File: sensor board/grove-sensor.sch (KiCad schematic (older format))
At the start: 28 parts, among them P1 CONN_01X03, P2 CONN_01X03, P3 CONN_01X03, P4 CONN_01X04, Q1 PN2222A, U1 ADD8704, U2 SI1143, U3 Teensy_3.1

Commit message: bunch of sensor stuff
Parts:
- removed P1, P2, P3: CONN_01X03, symbol CONN_01X03
- removed P4: CONN_01X04, symbol CONN_01X04
- added P1, P10, P11, P12, P13, P2, P3, P4, P5, P6, P7, P8, P9: CONN_01X01, Pin_Headers:Pin_Header_Straight_1x01, symbol CONN_01X01
- C1, C2, C3: footprint (none) -> Capacitors_SMD:C_0603_HandSoldering
- D1, D2, D3: footprint (none) -> LEDs:LED_0805
- Q1: footprint (none) -> TO_SOT_Packages_SMD:SOT-23_Handsoldering
- R1, R10, R11, R12, R13, R14, R3, R4, R6, R7, R8, R9: footprint (none) -> Resistors_SMD:R_0603_HandSoldering
- R2, R5: footprint (none) -> Resistors_SMD:R_0402
- U1: footprint (none) -> SI1143:TSSOP-14
- U2: footprint (none) -> SI1143:SI1143
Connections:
- wire segments 97 -> 98

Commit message: Some fixes and placement changes
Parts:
- removed P2, P3, P4, P5, P6: CONN_01X01, Pin_Headers:Pin_Header_Straight_1x01, symbol CONN_01X01
- added D4, D5: LED_RGB, LEDs:LED_WS2812-PLCC6, symbol LED_RGB
- added R15, R16, R17, R18, R19, R20: 100, Resistors_SMD:R_0603_HandSoldering, symbol R
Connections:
- net +5V: no longer P1.1 (P1)
- net GND: now also D4.1 (RC), D4.2 (GC), D4.3 (BC), D5.1 (RC), D5.2 (GC), D5.3 (BC)
- net OUT: no longer C2.1, R13.2
- net PIR_IN: now reaches U3.20 (20/A6)
- net PIR_IN: now also P1.1 (P1)
- net LED1_R: now reaches U3.4 (4(RX))
- net LED1_R: now also R18.1
- net LED1_G: now reaches U3.5
- net LED1_G: now also R19.1
- net LED1_B: now reaches U3.6
- net LED1_B: now also R20.1
- net LED2_R: now reaches U3.7 (7(RX3))
- net LED2_R: now also R15.1
- net LED2_G: now reaches U3.8 (8(TX3))
- net LED2_G: now also R16.1
- net LED2_B: now reaches U3.9 (9(RX2))
- net LED2_B: now also R17.1
- net at R5.1, R6.2, U1.3 (+INA): now also R7.2
- net at R12.1, U1.8 (OUTC): now also C2.1, R13.2
- net PROX_INT: no longer names the net of U2.4 (INT)
- new net: D5.4 (BA), R20.2
- new net: D5.5 (GA), R19.2
- new net: D5.6 (RA), R18.2
- new net: D4.4 (BA), R17.2
- new net: D4.5 (GA), R16.2
- new net: D4.6 (RA), R15.2
- no-connect marks 2 -> 3
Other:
- moved on the sheet: P10, P11, P12, P13, R12

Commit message: Draft sensor route on 4 layers
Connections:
- net LED1_B: now also U3.4 (4(RX)); no longer U3.6
- net LED1_R: now also U3.6; no longer U3.4 (4(RX))
- net LED2_B: now also U3.7 (7(RX3)); no longer U3.9 (9(RX2))
- net LED2_R: now also U3.9 (9(RX2)); no longer U3.7 (7(RX3))
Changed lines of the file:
@@
 Wire Wire Line
 	9150 1150 9350 1150
-Text Label 7600 2500 0    60   ~ 0
+Text Label 7600 2800 0    60   ~ 0
 LED1_R
 Text Label 7600 2650 0    60   ~ 0
 LED1_G
-Text Label 7600 2800 0    60   ~ 0
+Text Label 7600 2500 0    60   ~ 0
 LED1_B
-Text Label 7600 2950 0    60   ~ 0
+Text Label 7600 3250 0    60   ~ 0
 LED2_R
 Text Label 7600 3100 0    60   ~ 0
 LED2_G
-Text Label 7600 3250 0    60   ~ 0
+Text Label 7600 2950 0    60   ~ 0
 LED2_B
 Wire Wire Line

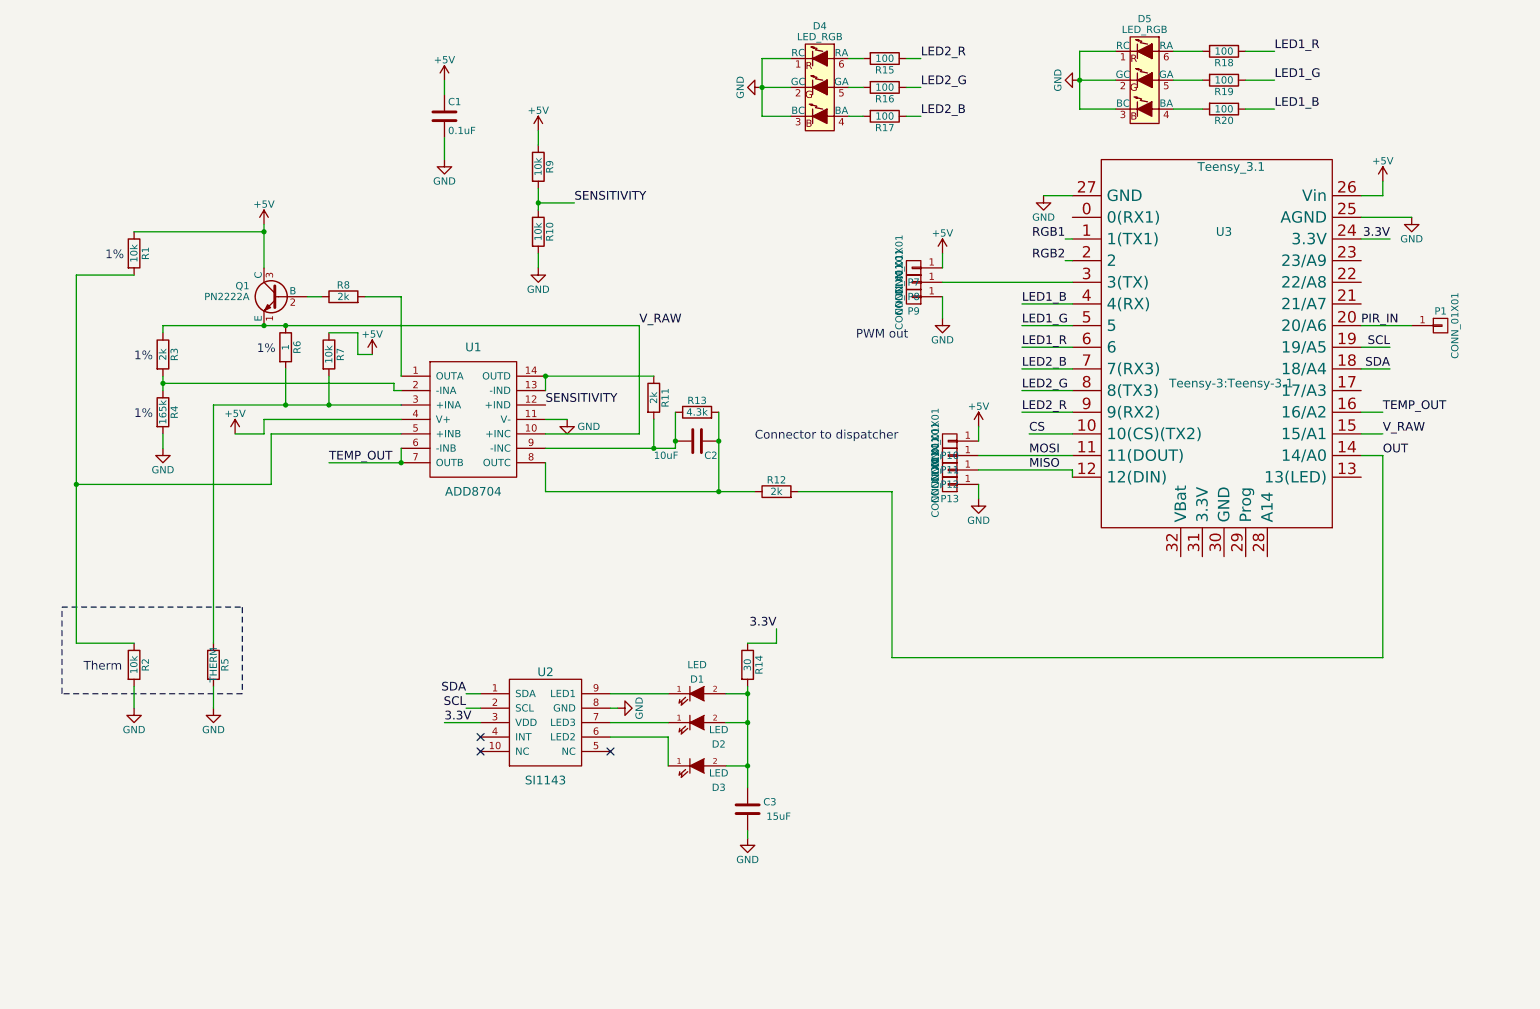
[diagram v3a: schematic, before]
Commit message: Fixes and updates to sensor board
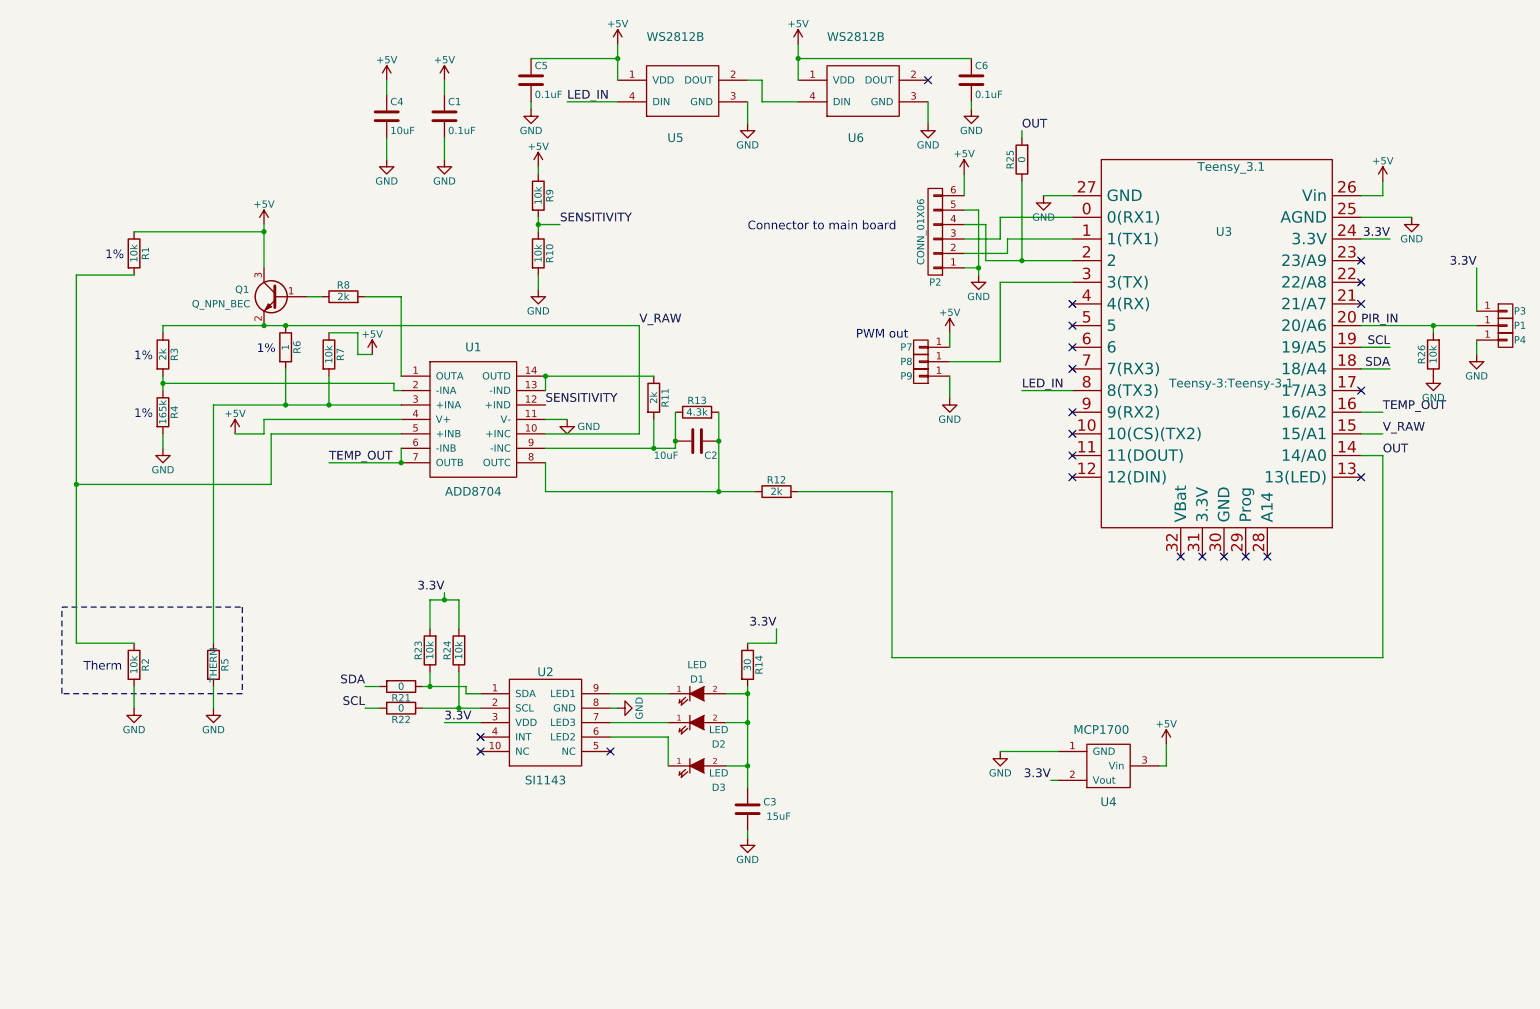
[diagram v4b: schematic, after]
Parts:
- removed D4, D5: LED_RGB, LEDs:LED_WS2812-PLCC6, symbol LED_RGB
- removed P10, P11, P12, P13: CONN_01X01, Pin_Headers:Pin_Header_Straight_1x01, symbol CONN_01X01
- removed Q1: PN2222A, TO_SOT_Packages_SMD:SOT-23_Handsoldering, symbol PN2222A
- removed R15, R16, R17, R18, R19, R20: 100, Resistors_SMD:R_0603_HandSoldering, symbol R
- added C4: 10uF, Capacitors_SMD:C_0603_HandSoldering, symbol C
- added C5, C6: 0.1uF, Capacitors_SMD:C_0603_HandSoldering, symbol C
- added P2: CONN_01X06, Pin_Headers:Pin_Header_Straight_1x06, symbol CONN_01X06
- added P3, P4: CONN_01X01, Pin_Headers:Pin_Header_Straight_1x01, symbol CONN_01X01
- added Q1: Q_NPN_BEC, TO_SOT_Packages_SMD:SOT-23, symbol Q_NPN_BEC
- added R21, R22, R25: 0, Resistors_SMD:R_0603_HandSoldering, symbol R
- added R23, R24, R26: 10k, Resistors_SMD:R_0603_HandSoldering, symbol R
- added U4: MCP1700, TO_SOT_Packages_SMD:SOT-23, symbol MCP1700
- added U5, U6: WS2812B, LEDs:LED_WS2812B-PLCC4, symbol WS2812B
- R2: footprint Resistors_SMD:R_0402 -> Resistors_SMD:R_0603
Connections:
- net +5V: now also C4.1, C5.1, C6.1, P2.6 (P6), Q1.3 (C), U4.3 (Vin), U5.1 (VDD), U6.1 (VDD)
- net 3.3V: now also P3.1 (P1), R23.2, R24.2, U4.2 (Vout)
- net GND: now also C4.2, C5.2, C6.2, P2.1 (P1), P2.5 (P5), P4.1 (P1), R26.1, U4.1 (GND), U5.3 (GND), U6.3 (GND)
- net OUT: now also R25.2
- net PIR_IN: now also R26.2
- net SCL: now also R22.2; no longer U2.2 (SCL)
- net SDA: now also R21.2; no longer U2.1 (SDA)
- net V_RAW: now also Q1.2 (E)
- net at U3.0 (0(RX1)): now also P2.3 (P3)
- net at R8.1: now also Q1.1 (B)
- net CS: no longer names the net of U3.10 (10(CS)(TX2))
- net LED1_B: no longer names the net of U3.4 (4(RX))
- net LED1_G: no longer names the net of U3.5
- net LED1_R: no longer names the net of U3.6
- net LED2_B: no longer names the net of U3.7 (7(RX3))
- net LED2_G renamed LED_IN
- net LED_IN: now also U5.4 (DIN)
- net LED2_R: no longer names the net of U3.9 (9(RX2))
- net MISO: no longer names the net of U3.12 (12(DIN))
- net MOSI: no longer names the net of U3.11 (11(DOUT))
- net RGB1: no longer names the net of U3.1 (1(TX1))
- net RGB1: now also P2.2 (P2)
- net RGB2: no longer names the net of U3.2
- net RGB2: now also P2.4 (P4), R25.1
- new net: R21.1, R23.1, U2.1 (SDA)
- new net: R22.1, R24.1, U2.2 (SCL)
- new net: U5.2 (DOUT), U6.4 (DIN)
- no-connect marks 3 -> 22
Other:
- note added: "Connector to main board\n"
- note removed: "Connector to dispatcher"
- moved on the sheet: P1, P7, P8, P9, R10, R9

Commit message: Changes for rev 2 of sensor board
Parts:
- removed P1, P3, P4, P7, P8, P9: CONN_01X01, Pin_Headers:Pin_Header_Straight_1x01, symbol CONN_01X01
- added P1, P3: CONN_01X03, Pin_Headers:Pin_Header_Straight_1x03, symbol CONN_01X03
- added P5, P6: CONN_01X01, Pin_Headers:Pin_Header_Straight_1x01, symbol CONN_01X01
- added R15: 300, Resistors_SMD:R_0603_HandSoldering, symbol R
- C4: value 10uF -> 100uF; footprint Capacitors_SMD:C_0603_HandSoldering -> Capacitors_SMD:C_1210_HandSoldering
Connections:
- net +5V: now also P1.3 (P3), P3.1 (P1)
- net GND: now also P1.1 (P1), P3.3 (P3)
- net LED_IN: now also R15.1; no longer U3.8 (8(TX3))
- net PIR_IN: now also P3.2 (P2)
- net at U3.3 (3(TX)): now also P1.2 (P2)
- new net: R15.2, U3.8 (8(TX3))
- no-connect marks 22 -> 24
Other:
- note added: "Mounting holes (M3)\n"
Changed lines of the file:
@@
 	1    0    0    -1
 $EndComp
-Text Notes 6450 2750 0    60   ~ 0
+Text Notes 6350 2950 0    60   ~ 0
 PWM out\n
 $Comp
@@
 	1    0    0    -1
 $EndComp
-$Comp
-L CONN_01X01 P7
-U 1 1 576CE696
-P 6900 2800
-F 0 "P7" H 7000 2800 50  0000 C CNN
-F 1 "CONN_01X01" H 7300 2800 50  0001 C CNN
-F 2 "Pin_Headers:Pin_Header_Straight_1x01" H 6900 2800 50  0001 C CNN
-F 3 "" H 6900 2800 50  0000 C CNN
-	1    6900 2800
-	-1   0    0    1
-$EndComp
-$Comp
-L CONN_01X01 P8
-U 1 1 576CE71E
-P 6900 2900
-F 0 "P8" H 7000 2900 50  0000 C CNN
-F 1 "CONN_01X01" H 7300 2900 50  0001 C CNN
-F 2 "Pin_Headers:Pin_Header_Straight_1x01" H 6900 2900 50  0001 C CNN
-F 3 "" H 6900 2900 50  0000 C CNN
-	1    6900 2900
-	-1   0    0    1
-$EndComp
-$Comp
-L CONN_01X01 P9
-U 1 1 576CE79F
-P 6900 3000
-F 0 "P9" H 7000 3000 50  0000 C CNN
-F 1 "CONN_01X01" H 7300 3000 50  0001 C CNN
-F 2 "Pin_Headers:Pin_Header_Straight_1x01" H 6900 3000 50  0001 C CNN
-F 3 "" H 6900 3000 50  0000 C CNN
-	1    6900 3000
-	-1   0    0    1
-$EndComp
 NoConn ~ 3850 5500
 Text Label 9950 2650 0    60   ~ 0
 PIR_IN
-$Comp
-L CONN_01X01 P1
-U 1 1 577554A8
-P 10950 2650
-F 0 "P1" H 11050 2650 50  0000 C CNN
-F 1 "CONN_01X01" V 11050 2650 50  0001 C CNN
-F 2 "Pin_Headers:Pin_Header_Straight_1x01" H 10950 2650 50  0001 C CNN
-F 3 "" H 10950 2650 50  0000 C CNN
-	1    10950 2650
-	1    0    0    -1
-$EndComp
 NoConn ~ 9950 3700
 NoConn ~ 9950 3100
@@
 P 3200 1200
 F 0 "C4" H 3225 1300 50  0000 L CNN
-F 1 "10uF" H 3225 1100 50  0000 L CNN
-F 2 "Capacitors_SMD:C_0603_HandSoldering" H 3238 1050 50  0001 C CNN
+F 1 "100uF" H 3225 1100 50  0000 L CNN
+F 2 "Capacitors_SMD:C_1210_HandSoldering" H 3238 1050 50  0001 C CNN
 F 3 "" H 3200 1200 50  0000 C CNN
 	1    3200 1200
@@
 	1    0    0    -1
 $EndComp
-$Comp
-L CONN_01X01 P3
-U 1 1 577CE261
-P 10950 2550
-F 0 "P3" H 11050 2550 50  0000 C CNN
-F 1 "CONN_01X01" V 11050 2550 50  0001 C CNN
-F 2 "Pin_Headers:Pin_Header_Straight_1x01" H 10950 2550 50  0001 C CNN
-F 3 "" H 10950 2550 50  0000 C CNN
-	1    10950 2550
-	1    0    0    -1
-$EndComp
-$Comp
-L CONN_01X01 P4
-U 1 1 577CE313
-P 10950 2750
-F 0 "P4" H 11050 2750 50  0000 C CNN
-F 1 "CONN_01X01" V 11050 2750 50  0001 C CNN
-F 2 "Pin_Headers:Pin_Header_Straight_1x01" H 10950 2750 50  0001 C CNN
-F 3 "" H 10950 2750 50  0000 C CNN
-	1    10950 2750
-	1    0    0    -1
-$EndComp
-Text Label 10750 2250 2    60   ~ 0
-3.3V
 $Comp
 L GND #PWR023
@@
 	7250 800  6050 800
 Connection ~ 6050 800
-Text Label 7600 3100 0    60   ~ 0
+Text Label 7250 3100 0    60   ~ 0
 LED_IN
 Wire Wire Line
-	7600 3100 7950 3100
+	7900 3100 7950 3100
 NoConn ~ 7950 3250
 NoConn ~ 7950 2950
@@
 	-1   0    0    -1
 $EndComp
+$Comp
+L CONN_01X01 P5
+U 1 1 57840858
+P 850 750
+F 0 "P5" H 950 750 50  0000 C CNN
+F 1 "CONN_01X01" H 1250 750 50  0001 C CNN
+F 2 "Pin_Headers:Pin_Header_Straight_1x01" H 850 750 118 0001 C CNN
+F 3 "" H 850 750 50  0000 C CNN
+	1    850  750
+	-1   0    0    1
+$EndComp
+$Comp
+L CONN_01X01 P6
+U 1 1 57840E70
+P 850 900
+F 0 "P6" H 950 900 50  0000 C CNN
+F 1 "CONN_01X01" H 1250 900 50  0001 C CNN
+F 2 "Pin_Headers:Pin_Header_Straight_1x01" H 850 900 118 0001 C CNN
+F 3 "" H 850 900 50  0000 C CNN
+	1    850  900
+	-1   0    0    1
+$EndComp
+Text Notes 600  650  0    60   ~ 0
+Mounting holes (M3)\n
+NoConn ~ 1050 750
+NoConn ~ 1050 900
+$Comp
+L CONN_01X03 P1
+U 1 1 579B74D1
+P 6900 2900
+F 0 "P1" H 6900 3100 50  0000 C CNN
+F 1 "CONN_01X03" V 7000 2900 50  0000 C CNN
+F 2 "Pin_Headers:Pin_Header_Straight_1x03" H 6900 2900 50  0001 C CNN
+F 3 "" H 6900 2900 50  0000 C CNN
+	1    6900 2900
+	-1   0    0    1
+$EndComp
+$Comp
+L CONN_01X03 P3
+U 1 1 579B7592
+P 10950 2650
+F 0 "P3" H 10950 2850 50  0000 C CNN
+F 1 "CONN_01X03" V 11050 2650 50  0000 C CNN
+F 2 "Pin_Headers:Pin_Header_Straight_1x03" H 10950 2650 50  0001 C CNN
+F 3 "" H 10950 2650 50  0000 C CNN
+	1    10950 2650
+	1    0    0    -1
+$EndComp
+$Comp
+L R R15
+U 1 1 579BC9AF
+P 7750 3100
+F 0 "R15" V 7830 3100 50  0000 C CNN
+F 1 "300" V 7750 3100 50  0000 C CNN
+F 2 "Resistors_SMD:R_0603_HandSoldering" V 7680 3100 50  0001 C CNN
+F 3 "" H 7750 3100 50  0000 C CNN
+	1    7750 3100
+	0    -1   -1   0
+$EndComp
+Wire Wire Line
+	7600 3100 7250 3100
+$Comp
+L +5V #PWR033
+U 1 1 579C073C
+P 10750 2250
+F 0 "#PWR033" H 10750 2100 50  0001 C CNN
+F 1 "+5V" H 10750 2390 50  0000 C CNN
+F 2 "" H 10750 2250 50  0000 C CNN
+F 3 "" H 10750 2250 50  0000 C CNN
+	1    10750 2250
+	1    0    0    -1
+$EndComp
 $EndSCHEMATC

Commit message: Added ultrasound to sensor and fixed plane short
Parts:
- added P4: CONN_01X07, Pin_Headers:Pin_Header_Straight_1x07, symbol CONN_01X07
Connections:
- net +5V: now also P1.2 (P2), P4.2 (P2); no longer P1.3 (P3)
- net GND: now also P4.1 (P1)
- net Ultrasound: now reaches U3.17 (17/A3)
- net Ultrasound: now also P4.5 (P5)
- net at U3.3 (3(TX)): now also P1.3 (P3); no longer P1.2 (P2)
- no-connect marks 24 -> 27
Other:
- moved on the sheet: P1, R26
